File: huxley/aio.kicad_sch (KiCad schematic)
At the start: 45 parts, among them J11 SMA_RF2-04A-T-00-50-G, J13 SMA_RF2-04A-T-00-50-G, J15 SMA_RF2-04A-T-00-50-G, J17 SMA_RF2-04A-T-00-50-G, J18 SMA_RF2-04A-T-00-50-G, J19 SMA_RF2-04A-T-00-50-G, J20 SMA_RF2-04A-T-00-50-G, J22 SMA_RF2-04A-T-00-50-G, J24 CT3151V1-2, J39 CT3151V1-2, J4 SMA_RF2-04A-T-00-50-G, J7 SMA_RF2-04A-T-00-50-G, J9 SMA_RF2-04A-T-00-50-G

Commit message: layout_1010
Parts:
- removed C40: 10u, Capacitor_SMD:C_0603_1608Metric, symbol pspice:C
- removed C41: 0.1u, Capacitor_SMD:C_0603_1608Metric, symbol pspice:C
- removed C42: 1n, Capacitor_SMD:C_0603_1608Metric, symbol pspice:C
- removed C43: 10p, Capacitor_SMD:C_0603_1608Metric, symbol pspice:C
- added C40: 10u, Capacitor_SMD:C_0603_1608Metric, symbol Device:C_Small
- added C41: 1u, Capacitor_SMD:C_0603_1608Metric, symbol Device:C_Small
- added C42, C43: 0.1u, Capacitor_SMD:C_0603_1608Metric, symbol Device:C_Small
- added C60, C61: 1n, Capacitor_SMD:C_0603_1608Metric, symbol Device:C_Small
- added C62, C63: 10p, Capacitor_SMD:C_0603_1608Metric, symbol Device:C_Small
- added C64, C65, C66, C67, C68, C69, C70, C71, C72, C73, C74, C75: x, Capacitor_SMD:C_0603_1608Metric, symbol Device:C_Small
- C1, C10, C11, C12, C2, C3, C4, C5, C6, C7, C8, C9: footprint Capacitor_SMD:C_0402_1005Metric -> Capacitor_SMD:C_0603_1608Metric
- C36, C37, C38, C39: symbol pspice:C -> Device:C_Small
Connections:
- net GND: now also C40.2, C41.2, C42.2, C43.2, C60.2, C61.2, C62.2, C63.2, C64.2, C65.2, C66.2, C67.2, C68.2, C69.2, C70.2, C71.2, C72.2, C73.2, C74.2, C75.2
- net output_0a: now also C65.1
- net output_0b: now also C64.1
- net output_1a: now also C66.1
- net output_1b: now also C67.1
- net output_2a: now also C68.1
- net output_2b: now also C69.1
- net output_3a: now also C70.1
- net output_3b: now also C71.1
- net output_4a: now also C72.1
- net output_4b: now also C73.1
- net output_5a: now also C74.1
- net output_5b: now also C75.1
- net vlvl: now also C40.1, C41.1, C42.1, C43.1, C60.1, C61.1, C62.1, C63.1
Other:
- moved on the sheet: C1, C10, C3, C5, C6, C9, J24, J39, R1, R10, R3, R5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

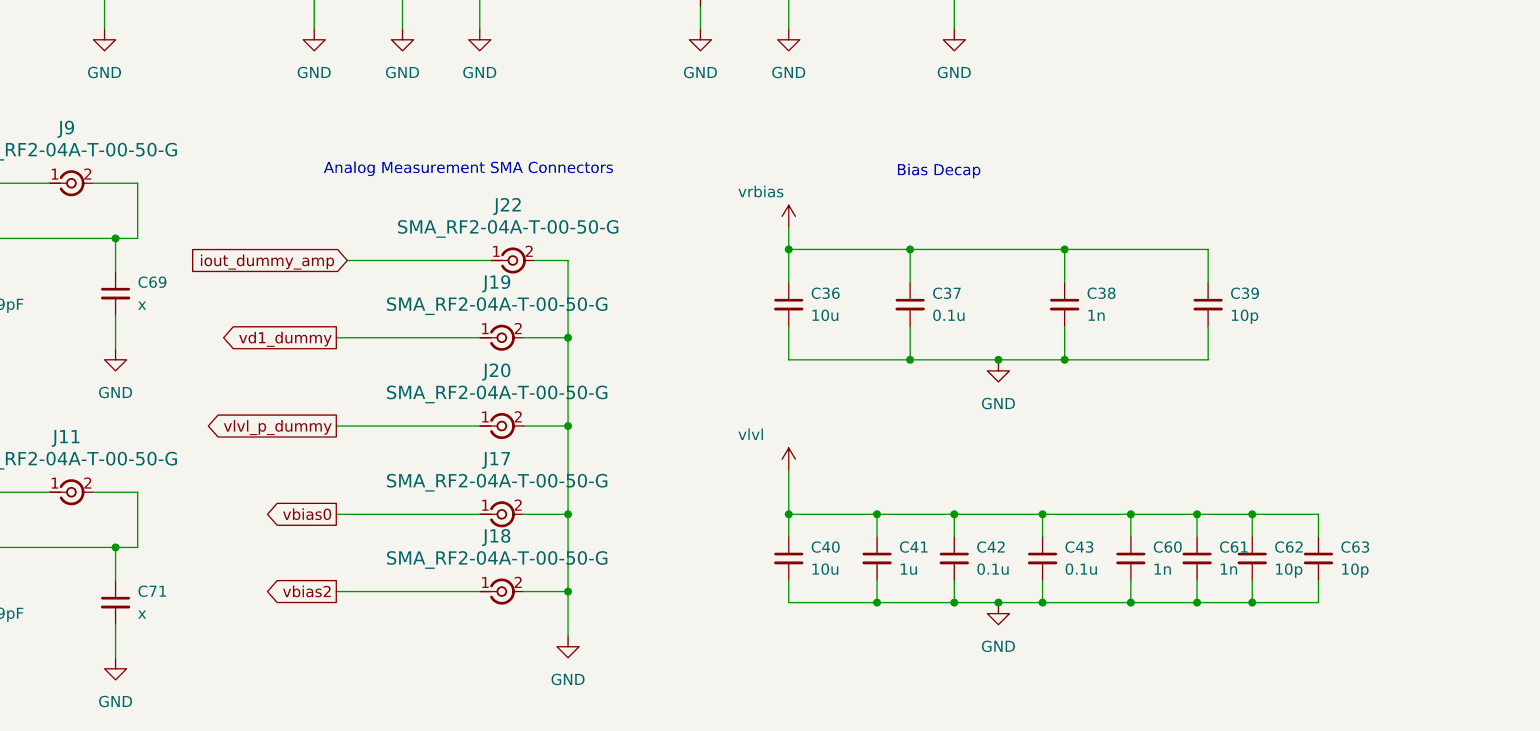
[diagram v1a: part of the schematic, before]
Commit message: minor schematic cleanup; addition of mounting holes; minor layout adjustment
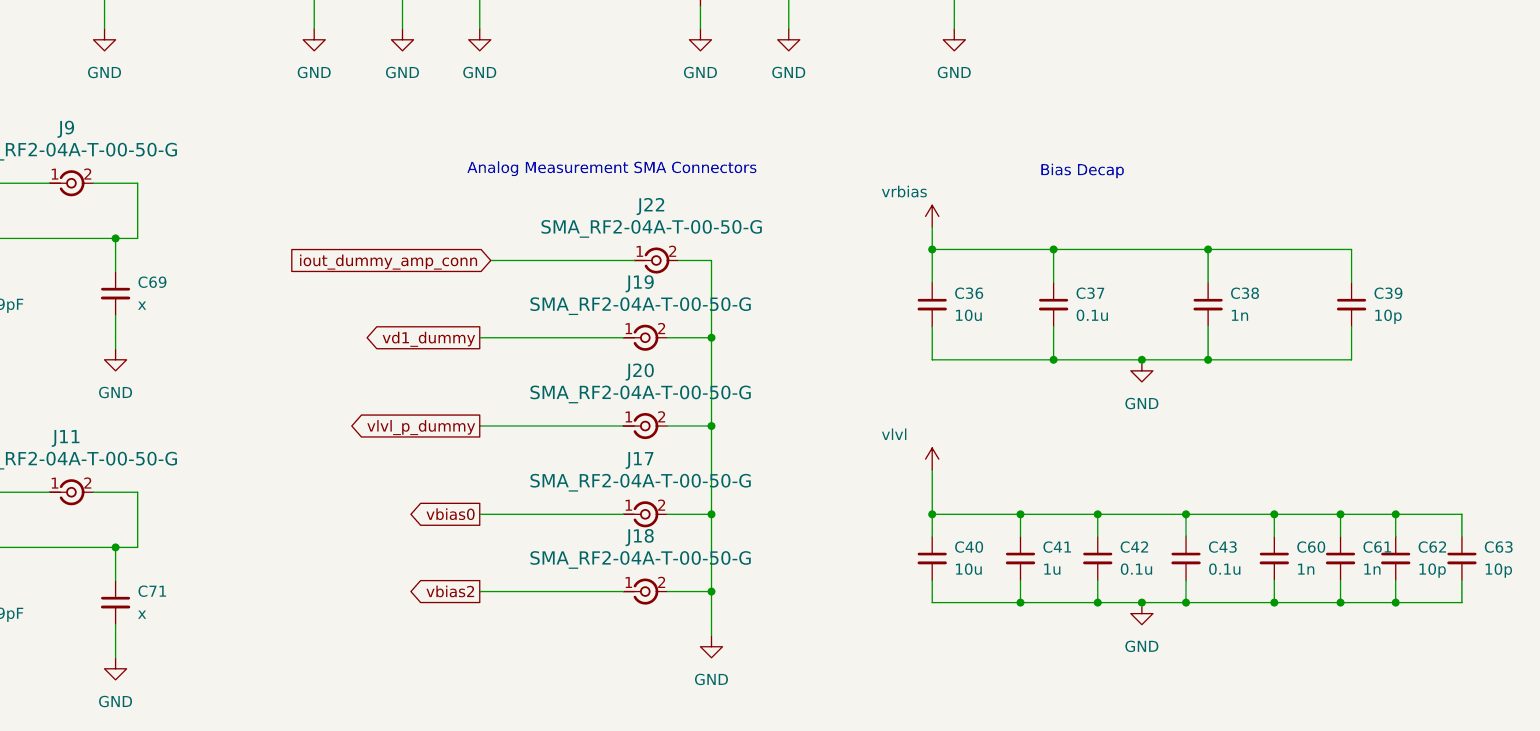
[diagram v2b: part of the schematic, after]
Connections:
- net iout_dummy_amp renamed iout_dummy_amp_conn
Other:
- moved on the sheet: C36, C37, C38, C39, C40, C41, C42, C43, C60, C61, C62, C63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

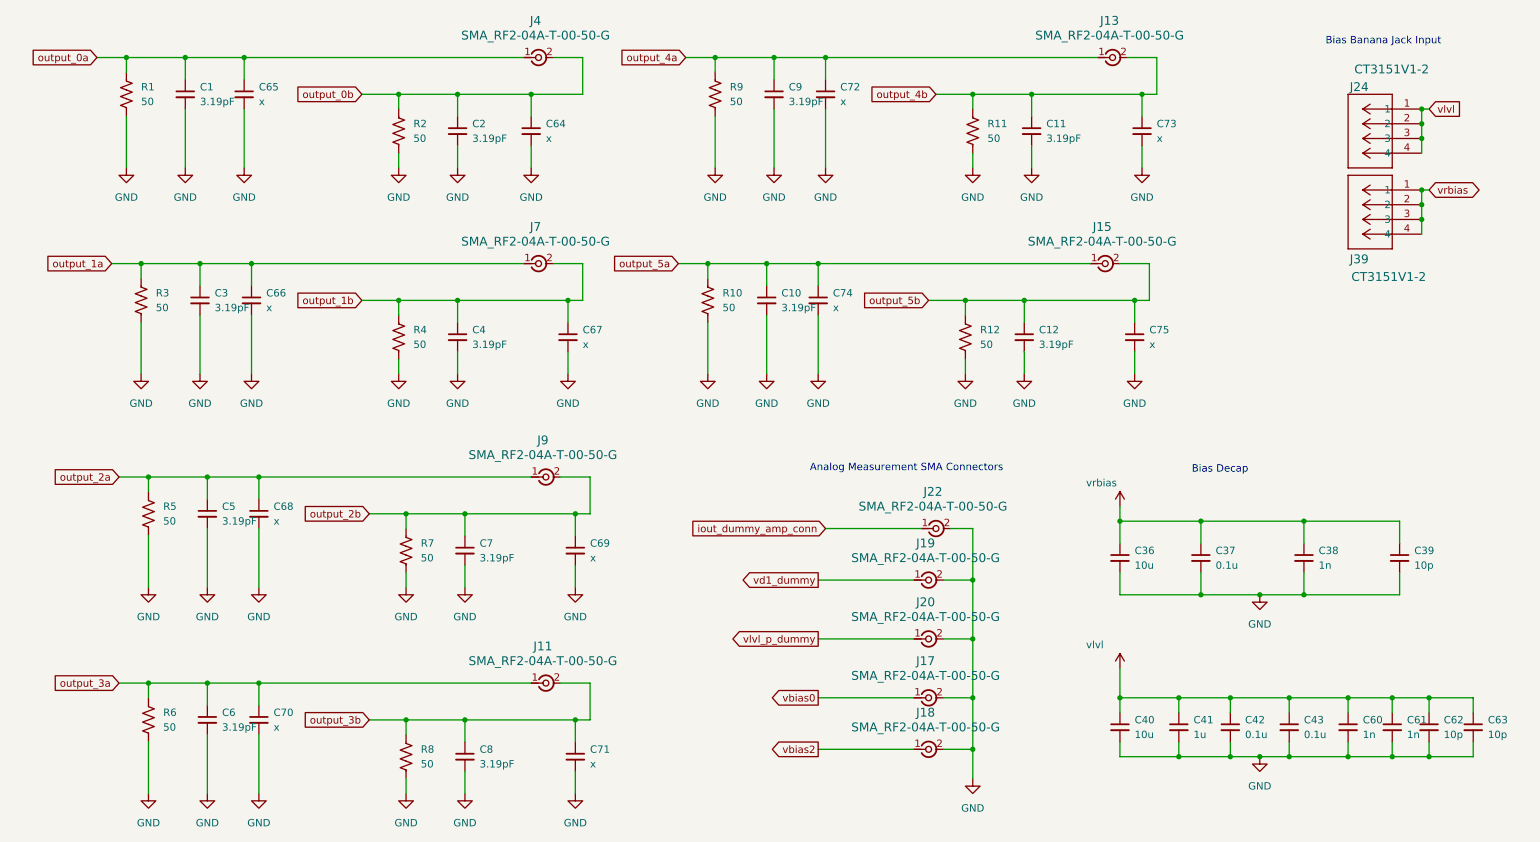
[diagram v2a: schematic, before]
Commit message: changed output names to be kicad diffpair-style (+/-); board rearrangement wip
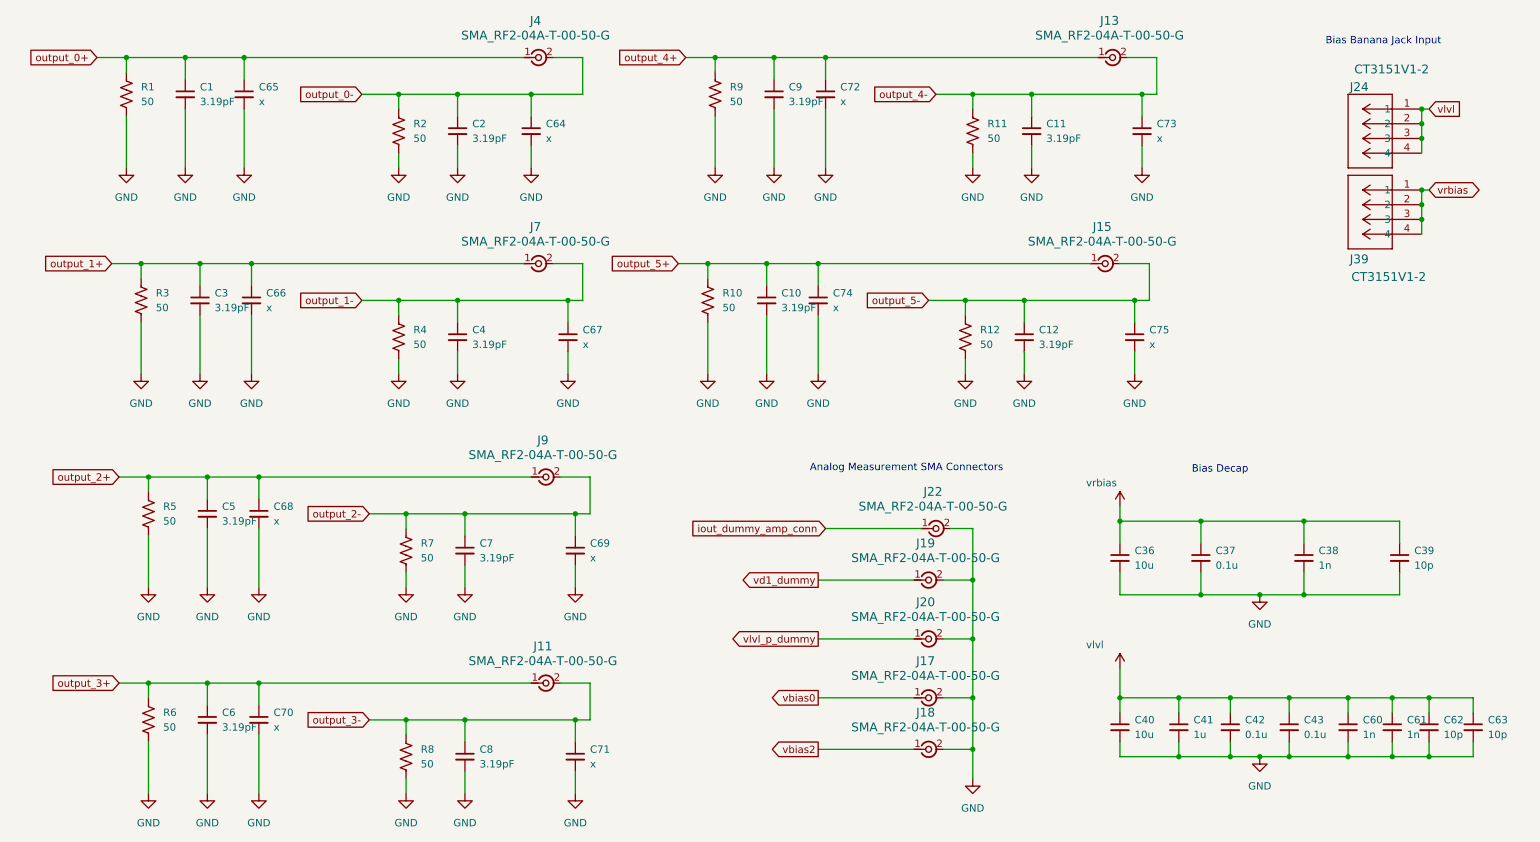
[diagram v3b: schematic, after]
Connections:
- net output_0a renamed output_0+
- net output_0b renamed output_0-
- net output_1a renamed output_1+
- net output_1b renamed output_1-
- net output_2a renamed output_2+
- net output_2b renamed output_2-
- net output_3a renamed output_3+
- net output_3b renamed output_3-
- net output_4a renamed output_4+
- net output_4b renamed output_4-
- net output_5a renamed output_5+
- net output_5b renamed output_5-
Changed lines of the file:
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@@
 		)
 	)
-	(global_label "output_3a"
+	(global_label "output_3+"
 		(shape input)
 		(at 35.56 139.7 180)
@@
 		)
 	)
-	(global_label "output_4b"
+	(global_label "output_4-"
 		(shape input)
 		(at 176.53 38.1 180)
@@
 		)
 	)
-	(global_label "output_5b"
+	(global_label "output_5-"
 		(shape input)
 		(at 175.26 73.66 180)
@@
 		)
 	)
-	(global_label "output_1a"
+	(global_label "output_1+"
 		(shape input)
 		(at 34.29 67.31 180)
@@
 		)
 	)
-	(global_label "output_0b"
+	(global_label "output_0-"
 		(shape input)
 		(at 77.47 38.1 180)
@@
 		)
 	)
-	(global_label "output_0a"
+	(global_label "output_0+"
 		(shape input)
 		(at 31.75 31.75 180)
@@
 		)
 	)
-	(global_label "output_1b"
+	(global_label "output_1-"
 		(shape input)
 		(at 77.47 73.66 180)
@@
 		)
 	)
-	(global_label "output_2b"
+	(global_label "output_2-"
 		(shape input)
 		(at 78.74 110.49 180)
@@
 		)
 	)
-	(global_label "output_5a"
+	(global_label "output_5+"
 		(shape input)
 		(at 132.08 67.31 180)
@@
 		)
 	)
-	(global_label "output_4a"
+	(global_label "output_4+"
 		(shape input)
 		(at 133.35 31.75 180)
@@
 		)
 	)
-	(global_label "output_3b"
+	(global_label "output_3-"
 		(shape input)
 		(at 78.74 146.05 180)
@@
 		)
 	)
-	(global_label "output_2a"
+	(global_label "output_2+"
 		(shape input)
 		(at 35.56 104.14 180)

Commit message: temp mid-rearrange
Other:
- note added: "For DC measurement???"
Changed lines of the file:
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@@
 	(text "Analog Measurement SMA Connectors"
 		(exclude_from_sim no)
-		(at 171.45 102.616 0)
+		(at 171.45 101.092 0)
 		(effects
 			(font
@@
 		(effects
 			(font
+				(size 1.27 1.27)
+			)
+		)
+	)
+	(text "For DC measurement???"
+		(exclude_from_sim no)
+		(at 171.45 103.632 0)
+		(effects
+			(font
